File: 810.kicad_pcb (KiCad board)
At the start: 4 copper layers, 148 x 105 mm, 329 parts, among them J1 PJ301BM, J10 PJ301BM, J11 PJ301BM, J12 PJ301BM, J13 PJ301BM, J14 PJ301BM, J15 JACK_MONO_SW, J16 PJ301BM, J17 PJ301B, J18 PJ301B, J2 PJ301BM, J3 PJ301BM, J4 PJ301B, J5 PJ301B, J6 PJ301BM, J7 PJ301BM, J8 PJ301BM, J9 PJ301BM, P1 CONN_01X08, P2 CONN_02X05, P3 CONN_01X03, P5 CONN_01X02, P6 CONN_02X03, Q1 PMBT2369, Q10 2SK208-GR, Q11 2SC4738, Q12 2SA1832, Q13 2SA1832, Q14 2SA1832, Q15 2SC4738, Q2 2SK208-GR, Q3 2SA1618, Q4 2SC4207, Q5 2SK208-GR, Q6 MMBF4391LT1G, Q7 2SA1832, Q8 PMBT2369, Q9 2SK208-GR, SW1 SPDT, SW2 SPDT, SW3 BF3-1050, SW4 SPDT, U1 TL072-, U10 TL072-, U11 TL072-, U12 TA75S558F, U13 TA75S558F, U14 TA75S558F, U15 TA75S558F, U16 TA75S558F, U17 CD4052, U18 TA75S558F, U19 TL072-, U2 TL072-, U20 CD4013, U21 TA75S558F, U3 TL072-, U4 CD40106, U5 CD4027, U6 LM13700, U7 LM13700, U8 LM13700, U9 TL072-

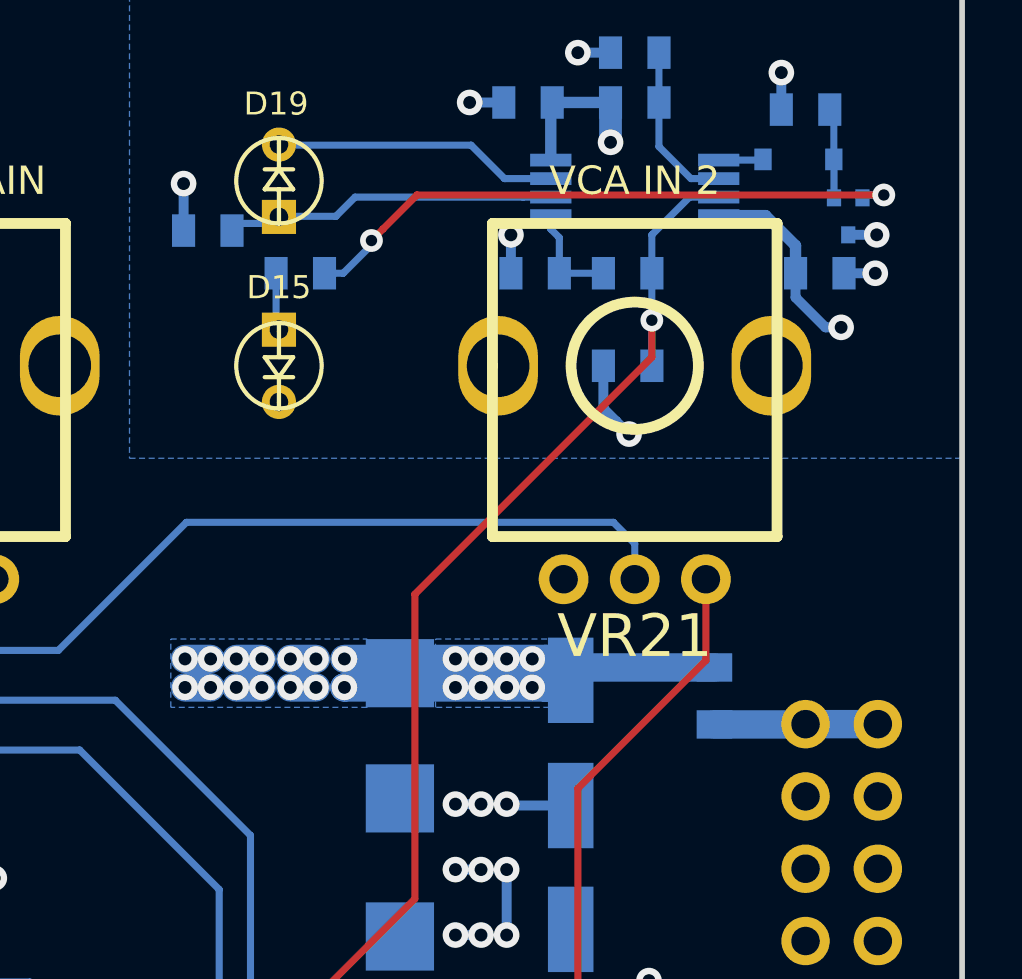
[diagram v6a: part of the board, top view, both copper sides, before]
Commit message: separate LED ground path
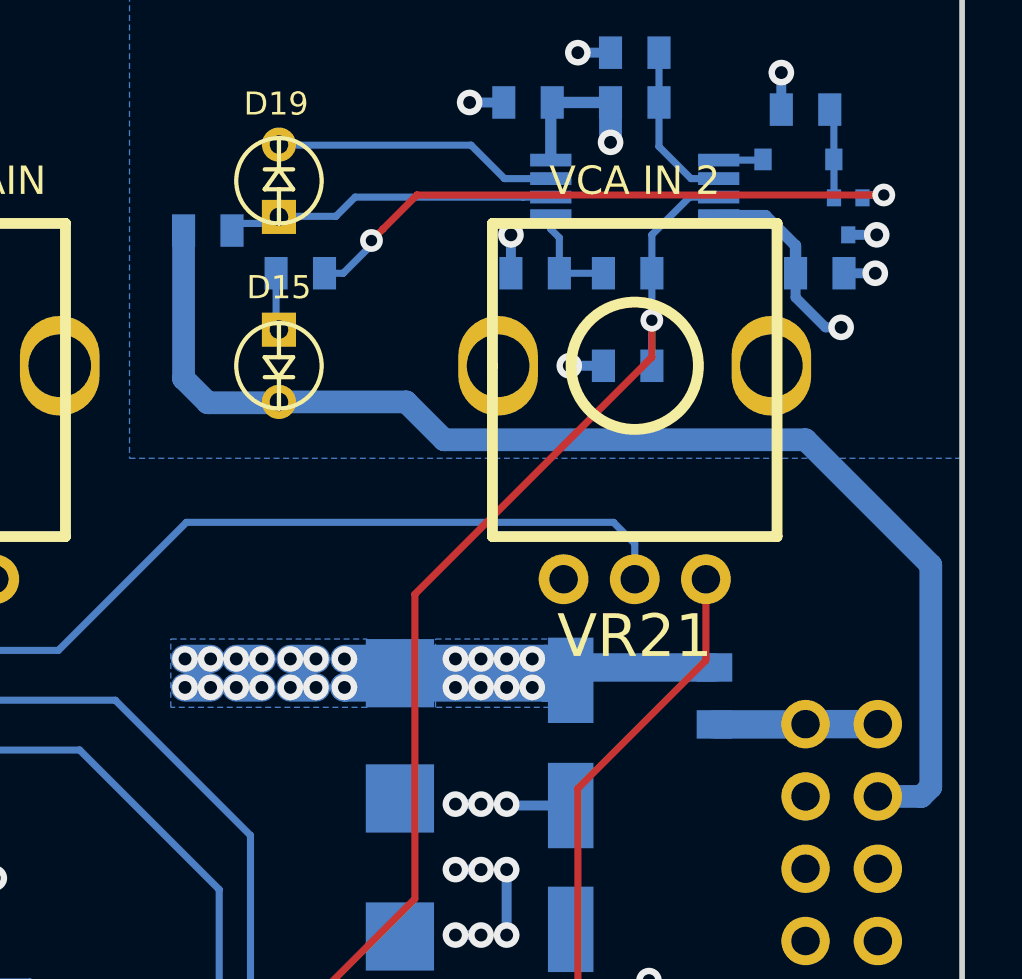
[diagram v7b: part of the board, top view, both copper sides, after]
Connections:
- D15 pad 1: GND -> /LED_GND
- P2 pad 8: GND -> /LED_GND
- R130 pad 1: GND -> /LED_GND
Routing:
- net /LED_GND: track 0.00 -> 44.0 mm
- net GND: track 123.9 -> 120.7 mm, vias 54 -> 53
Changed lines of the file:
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@@
 (kicad_pcb (version 4) (host pcbnew 4.0.2-stable)
   (general
-    (links 673)
+    (links 672)
     (no_connects 1)
     (area 83.899999 45.899999 232.100001 151.100001)
     (thickness 1.6)
     (drawings 135)
-    (tracks 2258)
+    (tracks 2264)
     (zones 0)
     (modules 329)
-    (nets 226)
+    (nets 227)
   )
   (page A4)
@@
     (0 F.Cu signal)
     (1 In1.Cu power hide)
-    (2 In2.Cu power hide)
+    (2 In2.Cu power)
     (31 B.Cu signal)
     (32 B.Adhes user)
@@
     (40 Dwgs.User user)
     (41 Cmts.User user)
-    (42 Eco1.User user)
+    (42 Eco1.User user hide)
     (43 Eco2.User user)
     (44 Edge.Cuts user)
@@
   )
   (setup
-    (last_trace_width 0.25)
+    (last_trace_width 0.8)
     (user_trace_width 0.25)
     (user_trace_width 0.4)
@@
   (net 224 "Net-(R125-Pad1)")
   (net 225 "Net-(R86-Pad2)")
+  (net 226 /LED_GND)
   (net_class Default "This is the default net class."
     (clearance 0.2)
@@
     (uvia_dia 0.3)
     (uvia_drill 0.1)
+    (add_net /LED_GND)
     (add_net Iabc)
     (add_net KYBD)
@@
       (net 10 GND))
     (pad 8 thru_hole oval (at 2.54 -7.62) (size 1.7 1.7) (drill 1) (layers *.Cu *.Mask)
-      (net 10 GND))
+      (net 226 /LED_GND))
     (pad 9 thru_hole oval (at 0 -10.16) (size 1.7 1.7) (drill 1) (layers *.Cu *.Mask)
       (net 61 "Net-(F1-Pad1)"))
@@
     (fp_line (start 0.5 -0.8) (end 1.4 -0.8) (layer B.SilkS) (width 0.2))
     (pad 1 smd rect (at -0.8509 0) (size 0.8128 1.143) (layers B.Cu B.Paste B.Mask)
-      (net 10 GND))
+      (net 226 /LED_GND))
     (pad 2 smd rect (at 0.8509 0) (size 0.8128 1.143) (layers B.Cu B.Paste B.Mask)
       (net 196 "Net-(D19-Pad2)"))
@@
       (net 60 "Net-(D15-Pad2)"))
     (pad 1 thru_hole circle (at 1.27 0 270) (size 1.2 1.2) (drill 0.65) (layers *.Cu *.Mask F.SilkS)
-      (net 10 GND))
+      (net 226 /LED_GND))
     (model "E:/Documents/KiCad/MyLibs/MyModules/3D models/VRML2/WP710A10ID-3MMLED.wrl"
       (at (xyz 0 0 0.254))
@@
   (segment (start 148.635 73.90158) (end 148.635 70.7159) (width 0.25) (layer B.Cu) (net 9))
   (segment (start 148.635 70.7159) (end 148.75 70.6009) (width 0.25) (layer B.Cu) (net 9))
+  (segment (start 219.3991 59) (end 218.2 59) (width 0.35) (layer B.Cu) (net 10))
+  (via (at 218.2 59) (size 0.9) (drill 0.45) (layers F.Cu B.Cu) (net 10))
   (segment (start 201.5491 117.9491) (end 201.6 118) (width 0.35) (layer B.Cu) (net 10))
   (segment (start 201.5491 116.8) (end 201.5491 117.9491) (width 0.35) (layer B.Cu) (net 10))
@@
   (segment (start 185.0509 83.1509) (end 185.05 83.15) (width 0.35) (layer B.Cu) (net 10))
   (via (at 185.05 83.15) (size 0.9) (drill 0.45) (layers F.Cu B.Cu) (net 10))
-  (segment (start 219.850001 60.950001) (end 220.3 61.4) (width 0.35) (layer B.Cu) (net 10))
-  (segment (start 219.3991 60.4991) (end 219.850001 60.950001) (width 0.35) (layer B.Cu) (net 10))
-  (segment (start 219.3991 59) (end 219.3991 60.4991) (width 0.35) (layer B.Cu) (net 10))
-  (via (at 220.3 61.4) (size 0.9) (drill 0.45) (layers F.Cu B.Cu) (net 10))
   (segment (start 216.1491 55.75) (end 216.1491 54.4009) (width 0.35) (layer B.Cu) (net 10))
   (segment (start 216.1491 54.4009) (end 216.15 54.4) (width 0.35) (layer B.Cu) (net 10))
@@
   (segment (start 227.8509 55.75) (end 228.95 55.75) (width 0.35) (layer B.Cu) (net 10))
   (via (at 228.95 55.75) (size 0.9) (drill 0.45) (layers F.Cu B.Cu) (net 10))
-  (segment (start 204.6491 54.25) (end 204.6491 52.6009) (width 0.35) (layer B.Cu) (net 10))
-  (segment (start 204.6491 52.6009) (end 204.65 52.6) (width 0.35) (layer B.Cu) (net 10))
-  (via (at 204.65 52.6) (size 0.9) (drill 0.45) (layers F.Cu B.Cu) (net 10))
   (segment (start 125.4 62) (end 126.4 62) (width 0.25) (layer F.Cu) (net 10))
   (segment (start 125.1 61.25) (end 125.1 61.7) (width 0.25) (layer F.Cu) (net 10))
@@
   (segment (start 195.5 128.45) (end 195.5 130.3509) (width 0.25) (layer B.Cu) (net 225))
   (segment (start 195.5 130.3509) (end 195.6491 130.5) (width 0.25) (layer B.Cu) (net 225))
+  (segment (start 208 60.27) (end 212.47 60.27) (width 0.8) (layer B.Cu) (net 226))
+  (segment (start 212.47 60.27) (end 213.8 61.6) (width 0.8) (layer B.Cu) (net 226))
+  (segment (start 213.8 61.6) (end 226.5 61.6) (width 0.8) (layer B.Cu) (net 226))
+  (segment (start 226.5 61.6) (end 230.9 66) (width 0.8) (layer B.Cu) (net 226))
+  (segment (start 230.9 66) (end 230.9 73.8) (width 0.8) (layer B.Cu) (net 226))
+  (segment (start 230.9 73.8) (end 230.57 74.13) (width 0.8) (layer B.Cu) (net 226))
+  (segment (start 230.57 74.13) (end 229.04 74.13) (width 0.8) (layer B.Cu) (net 226))
+  (segment (start 204.6491 54.25) (end 204.6491 59.4491) (width 0.8) (layer B.Cu) (net 226))
+  (segment (start 204.6491 59.4491) (end 205.5 60.3) (width 0.8) (layer B.Cu) (net 226))
+  (segment (start 205.5 60.3) (end 207.97 60.3) (width 0.8) (layer B.Cu) (net 226))
+  (segment (start 207.97 60.3) (end 208 60.27) (width 0.8) (layer B.Cu) (net 226))
   (zone (net 10) (net_name GND) (layer B.Cu) (hatch edge 0.508)
     (connect_pads (clearance 0.254))

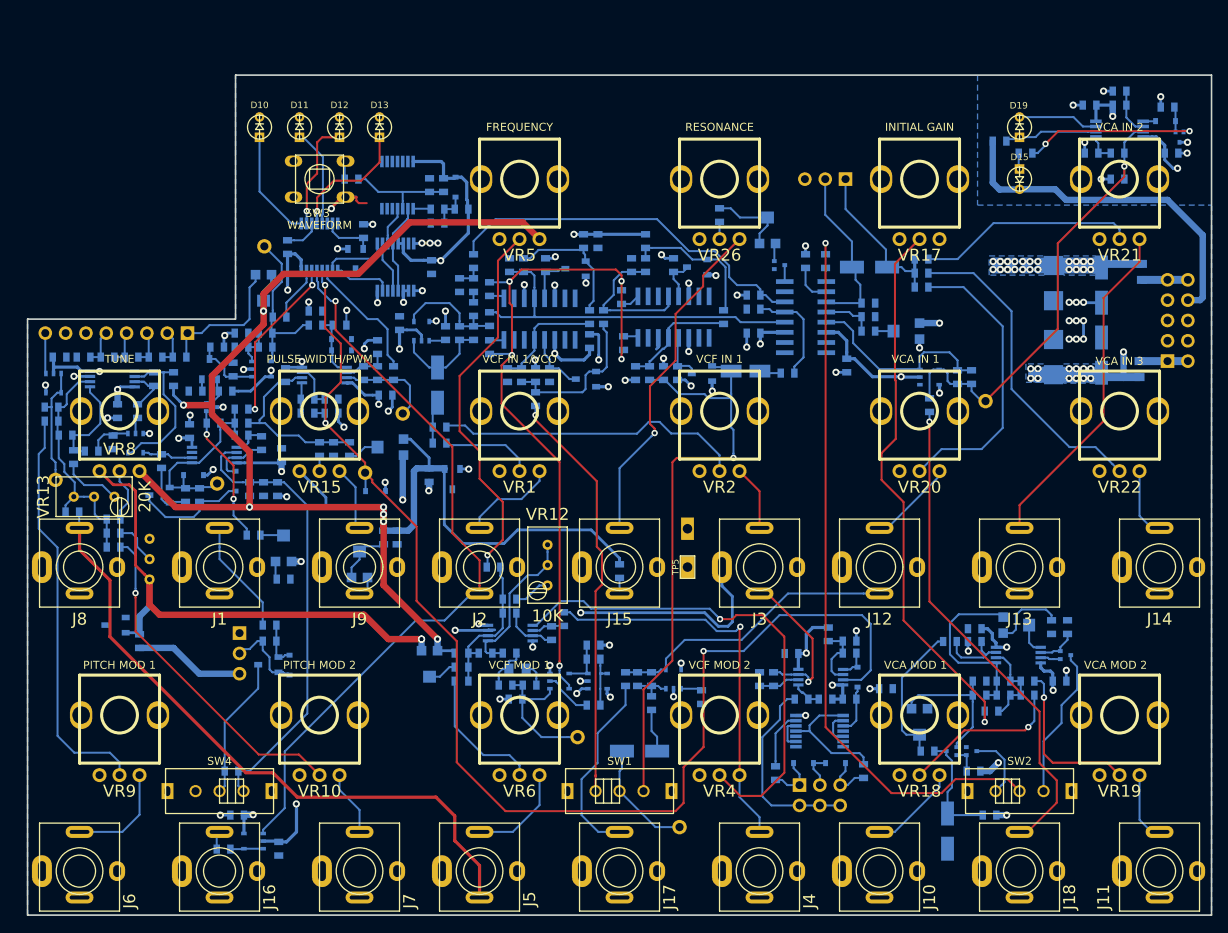
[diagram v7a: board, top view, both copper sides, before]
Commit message: 0603 R and C footprints swapped for reflow friendly footprints
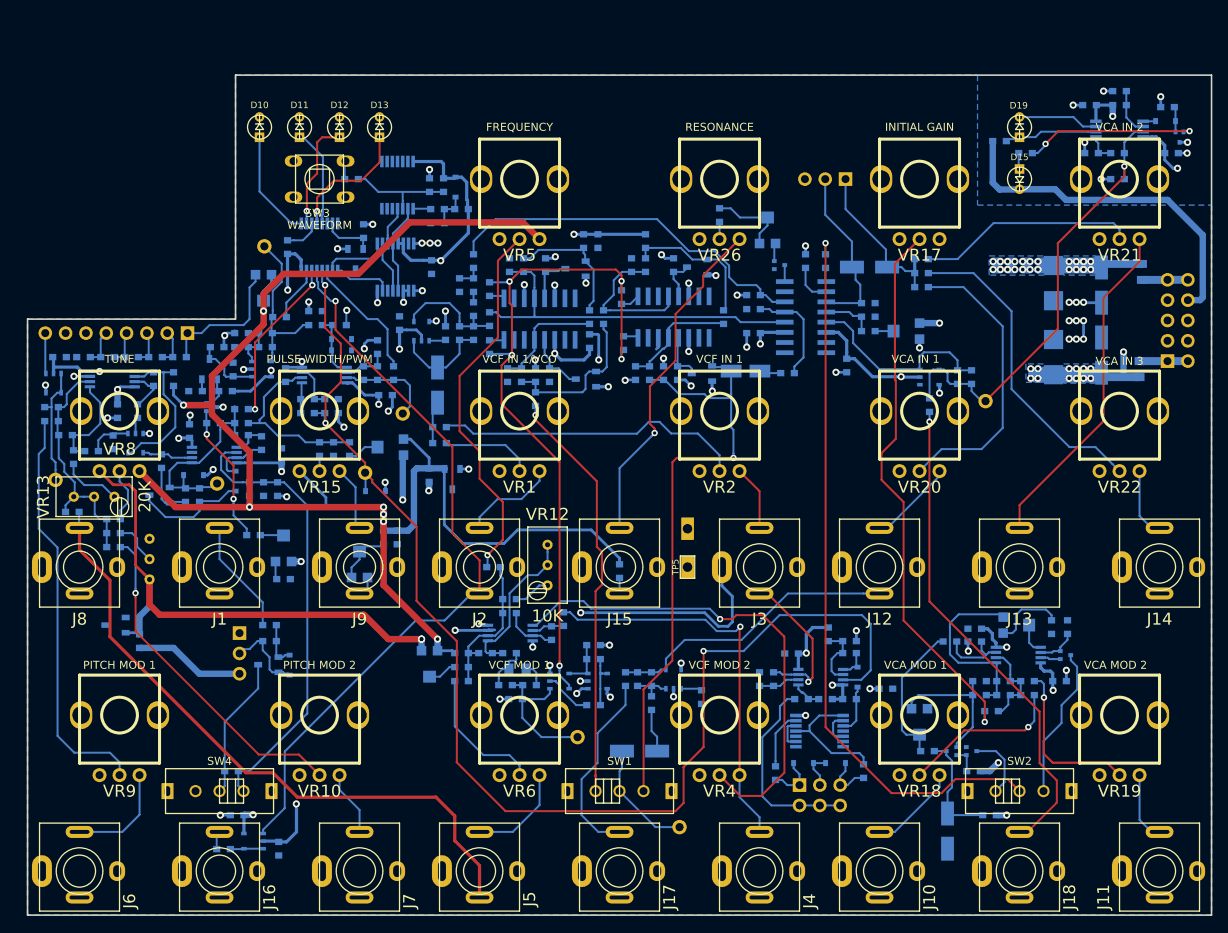
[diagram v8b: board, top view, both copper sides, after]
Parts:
- C1, C10, C11, C12, C13, C14, C16, C17, C18, C19, C20, C22, C24, C25, C27, C28, C29, C3, C30, C31, C32, C33, C34, C35, C36, C37, C38, C39, C4, C40, C41, C42, C43, C44, C47, C48, C49, C5, C50, C51, C6, C7, C8, C9: footprint MyModules:SM0603-C-JRL -> MyModules:SM0603-C-MURATA
- R1, R10, R100, R101, R102, R103, R104, R105, R106, R107, R108, R109, R11, R110, R111, R112, R113, R114, R115, R116, R117, R118, R119, R12, R120, R121, R122, R123, R124, R125, R126, R127, R128, R129, R13, R130, R131, R132, R133, R134, R135, R136, R137, R138, R139, R14, R140, R141, R142, R143, R144, R145, R146, R147, R148, R149, R15, R150, R16, R17, R18, R19, R2, R20, R21, R22, R23, R24, R25, R26, R27, R28, R29, R3, R30, R31, R32, R33, R34, R35, R36, R37, R39, R4, R40, R41, R42, R43, R44, R45, R46, R47, R48, R49, R5, R50, R51, R52, R53, R54, R55, R56, R57, R58, R59, R6, R60, R61, R62, R63, R64, R65, R66, R67, R68, R69, R7, R70, R71, R72, R73, R74, R75, R76, R77, R78, R79, R8, R80, R81, R82, R83, R84, R85, R86, R87, R88, R9, R90, R91, R92, R93, R94, R95, R96, R97, R98, R99, TC1: footprint MyModules:SM0603-R-JRL -> MyModules:SM0603-R-YAGEO
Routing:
- net GND: track 120.7 -> 115.2 mm
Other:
- board text added: "r1.3 10/18"
- board text removed: "r1.2 05/18"
